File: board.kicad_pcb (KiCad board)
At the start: 2 copper layers, 115.4 x 59.7 mm, 47 parts, among them J1 TEMPS, J2 OLED, J3 HV1, J4 HV2, J5 PWR_IN, J6 PROG, K1 RELAY1, K3 RELAY2, Q3 AO3400A, Q4 AO3400A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

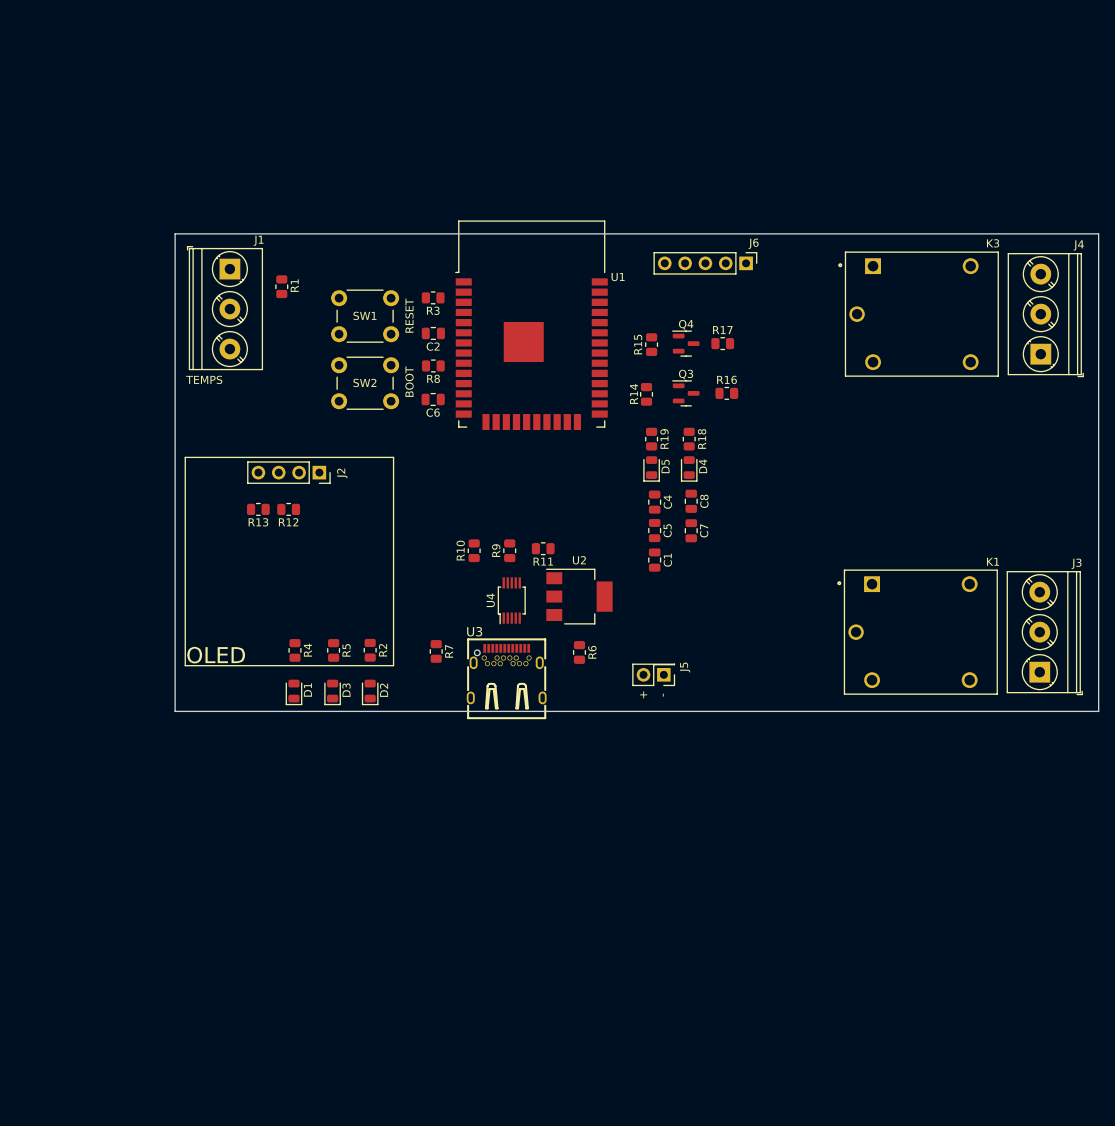
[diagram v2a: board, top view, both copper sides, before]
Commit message: feat: redesigned board for 5x5
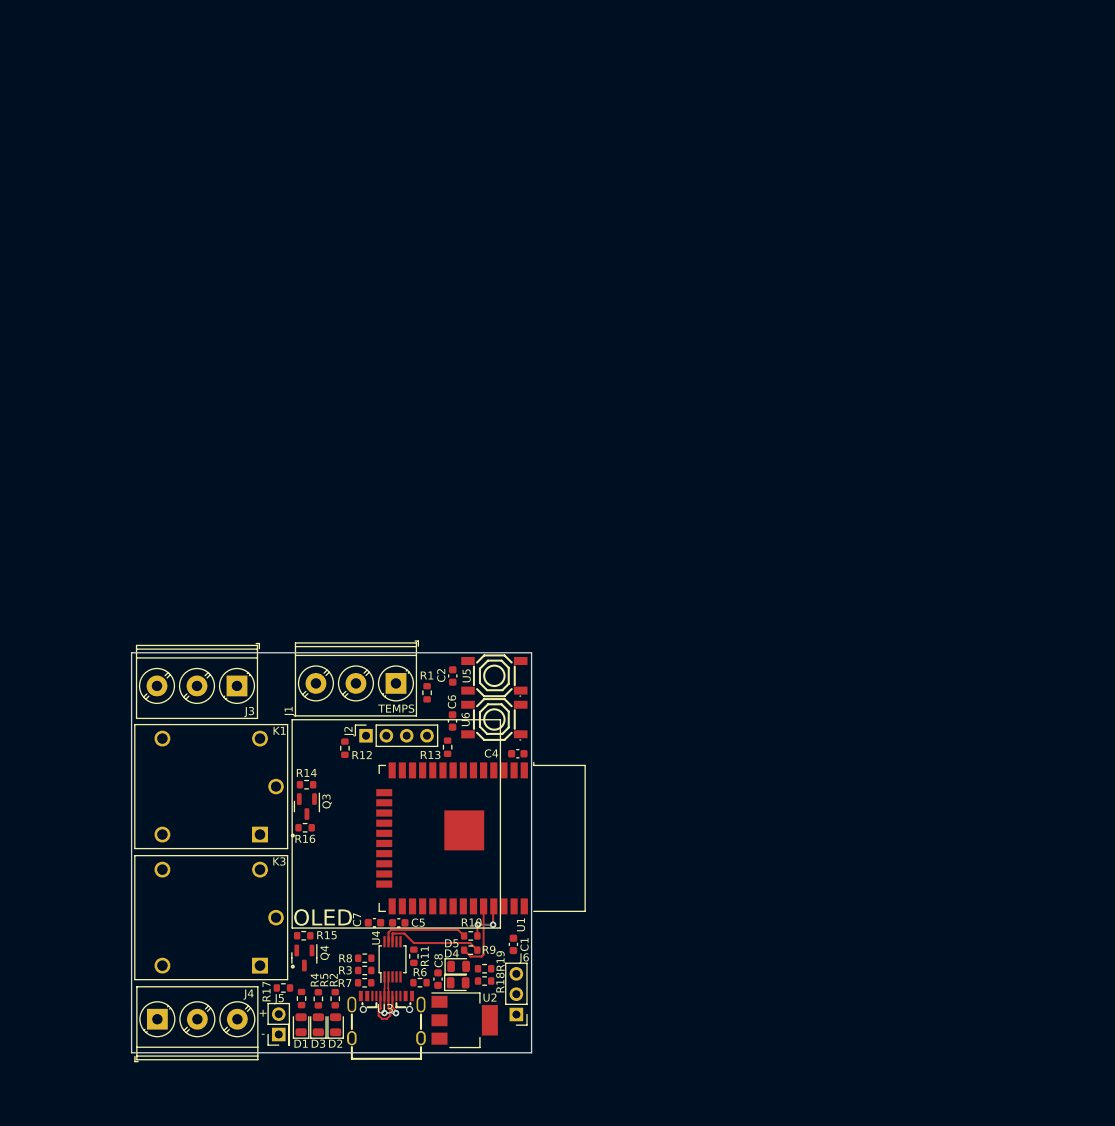
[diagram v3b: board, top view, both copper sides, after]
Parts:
- removed SW1: SW_RST, Button_Switch_THT:SW_PUSH_6mm_H4.3mm
- removed SW2: SW_BOOT, Button_Switch_THT:SW_PUSH_6mm_H4.3mm
- added U5: SW_RST, board:SW-SMD_4P-L5.1-W5.1-P3.70-LS6.5-TL-2, F.Cu at (99.8, 106.2)
- added U6: SW_BOOT, board:SW-SMD_4P-L5.1-W5.1-P3.70-LS6.5-TL-2, F.Cu at (99.8, 111.6)
- C1, C2, C4, C5, C6, C7, C8: footprint Capacitor_SMD:C_0805_2012Metric -> Capacitor_SMD:C_0603_1608Metric
- J6: footprint Connector_PinHeader_2.54mm:PinHeader_1x05_P2.54mm_Vertical -> Connector_PinHeader_2.54mm:PinHeader_1x03_P2.54mm_Vertical
- K1, K3: footprint SRD-05VDC-SL-C:RELAY_SRD-05VDC-SL-C -> board:RELAY_SRD-05VDC-SL-C
- R1, R10, R11, R12, R13, R14, R15, R16, R17, R18, R19, R2, R3, R4, R5, R6, R7, R8, R9: footprint Resistor_SMD:R_0805_2012Metric -> Resistor_SMD:R_0603_1608Metric
- U2: value AMS1117-3.3 -> AMS1117
- U3: value USB-306C -> USB3_1C16PFSMT; footprint board:USB-TYPE-C-TH_USB-306C -> board:USB-C-SMD_TYPE-C-USB-17
- moved J4 138.2 mm to (57.7, 149.1), turned to 0 degrees
- moved K3 116.5 mm to (64.5, 136.4), turned to 180 degrees
- moved J3 100.4 mm to (67.7, 107.4), turned to 180 degrees
- moved J6 98.2 mm to (102.6, 148.5), turned to 180 degrees
- moved R17 97.5 mm to (73.5, 145.2), turned to 180 degrees
- moved K1 90.8 mm to (64.5, 120.0), turned to 180 degrees
- moved Q4 90.4 mm to (76.1, 141.4), turned to -90 degrees
- moved R15 85.7 mm to (76.0, 138.7), turned to 0 degrees
- moved R3 84.5 mm to (83.7, 143.0), turned to 0 degrees
- moved R16 75.7 mm to (76.2, 125.2), turned to 180 degrees
- moved R8 74.5 mm to (83.7, 141.5), turned to 0 degrees
- moved R18 72.4 mm to (98.6, 144.3), turned to 180 degrees
- moved D4 70.6 mm to (95.3, 144.5), turned to 0 degrees
- moved Q3 70.1 mm to (76.4, 122.5), turned to -90 degrees
- moved R19 69.4 mm to (98.6, 142.8), turned to 180 degrees
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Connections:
- net /NCTS renamed NCTS
- net Net-(D4-Pad2) renamed /RXLED_V
- net Net-(D5-Pad2) renamed /TXLED_V
- net Net-(K1-PadA1) renamed /RELAY1_G1
- net Net-(K3-PadA1) renamed /RELAY2_G1
- net Net-(Q3-Pad3) renamed /RELAY1_G2
- net Net-(Q4-Pad3) renamed /RELAY2_G2
- J6 pad 1: +3V3 -> TX_ESP
- J6 pad 3: TX_ESP -> +3V3
- U3 pad A5: CC2 -> CC1
- U3 pad B5: CC1 -> CC2
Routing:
- net TX_CH: track 0.00 -> 12.5 mm
- net RX_CH: track 0.00 -> 11.1 mm
- net RX_ESP: track 0.00 -> 8.89 mm
- net D-: track 0.00 -> 8.53 mm
- net D+: track 0.00 -> 7.60 mm, vias 0 -> 2
- net TX_ESP: track 0.00 -> 5.66 mm, vias 0 -> 2
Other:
- board size 115.4 x 59.7 mm -> 50 x 50 mm
- copper layers 2 -> 4

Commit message: feat: initial routing
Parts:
- J3: value HV1 -> HV2
- J4: value HV2 -> HV1
- K1: value RELAY1 -> RELAY2
- K3: value RELAY2 -> RELAY1
- U2: value AMS1117 -> AMS1117-3.3
- U5, U6: footprint board:SW-SMD_4P-L5.1-W5.1-P3.70-LS6.5-TL-2 -> board:SW-SMD_L6.0-W3.5-LS8.0
- moved J5 12.3 mm to (78.8, 140.2), turned to 180 degrees
- moved R17 11.6 mm to (76.3, 133.9)
- moved Q4 10.2 mm to (76.5, 131.2)
- moved R15 10.2 mm to (76.5, 128.4)
- moved C6 5.53 mm to (93.6, 106.4), turned to 0 degrees
- moved U6 5.25 mm to (99.7, 106.4), turned to 0 degrees
- moved C2 4.16 mm to (93.6, 110.2), turned to 0 degrees
- moved U5 4.05 mm to (99.7, 110.2), turned to 0 degrees
- moved R8 2.46 mm to (82.8, 139.2)
- moved R3 2.45 mm to (82.8, 140.7)
- moved C8 2.15 mm to (92.8, 141.9)
- moved R1 1.85 mm to (91.3, 110.1)
- moved R12 1.24 mm to (81.0, 114.0)
- moved R13 1.12 mm to (93.8, 114.0)
- moved J2 0.64 mm to (83.6, 114.3)
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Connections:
- Q3 pad 1: CH1 -> CH2
- Q4 pad 1: CH2 -> CH1
- R14 pad 2: CH1 -> CH2
- R15 pad 2: CH2 -> CH1
- U5 pad 2: EN_ESP -> GND
- U6 pad 2: GPIO0 -> GND
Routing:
- net Net-(J3-Pad2): track 0.00 -> 103.2 mm
- net Net-(J4-Pad2): track 0.00 -> 100.9 mm
- net VBUS: track 0.00 -> 87.0 mm, vias 0 -> 1
- net Net-(J4-Pad1): track 0.00 -> 80.4 mm
- net Net-(J3-Pad3): track 0.00 -> 80.3 mm
- net GPIO0: track 0.00 -> 60.6 mm, vias 0 -> 2
- net EN_ESP: track 0.00 -> 51.3 mm, vias 0 -> 2
- net Net-(J4-Pad3): track 0.00 -> 48.1 mm
- net Net-(J3-Pad1): track 0.00 -> 48.0 mm
- net SCL: track 0.00 -> 43.0 mm, vias 0 -> 2
- net SLED2: track 0.00 -> 36.3 mm
- net SLED1: track 0.00 -> 34.7 mm
- net SDA: track 0.00 -> 30.5 mm, vias 0 -> 2
- net CH2: track 0.00 -> 29.6 mm, vias 0 -> 2
- net GPIO14: track 0.00 -> 27.0 mm
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
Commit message: feat: routed with planes and no warnings or errors
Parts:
- C1, C2, C4, C5, C6, C7, C8: footprint Capacitor_SMD:C_0603_1608Metric -> Capacitor_SMD:C_0402_1005Metric
- D1, D2, D3, D4, D5: footprint LED_SMD:LED_0805_2012Metric -> LED_SMD:LED_0603_1608Metric
- R1, R10, R11, R12, R13, R14, R15, R16, R17, R18, R19, R2, R3, R4, R5, R6, R7, R8, R9: footprint Resistor_SMD:R_0603_1608Metric -> Resistor_SMD:R_0402_1005Metric
- U3: value USB3_1C16PFSMT -> USBC
- moved J3 100.1 mm to (167.7, 107.1)
- moved K1 98.5 mm to (163.0, 120.2), turned to 0 degrees
- moved Q3 91.3 mm to (166.9, 134.9), turned to 90 degrees
- moved J1 90.8 mm to (167.5, 150.2), turned to 90 degrees
- moved R16 88.9 mm to (164.6, 133.9), turned to -90 degrees
- moved J4 88.2 mm to (135.2, 107.1), turned to 180 degrees
- moved R4 84.9 mm to (159.6, 133.1), turned to 180 degrees
- moved R1 81.8 mm to (162.4, 150.6)
- moved D1 79.6 mm to (153.1, 131.1), turned to 0 degrees
- moved R5 79.5 mm to (156.1, 133.1), turned to 180 degrees
- moved D3 77.2 mm to (153.1, 132.8), turned to 0 degrees
- moved R12 68.1 mm to (148.0, 125.7), turned to 0 degrees
- moved K3 68.0 mm to (130.4, 120.2), turned to 0 degrees
- moved J2 67.0 mm to (139.6, 151.1), turned to 180 degrees
- moved R14 66.5 mm to (139.5, 140.7), turned to -90 degrees
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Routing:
- net Net-(J4-Pad1): track 80.4 -> 34.9 mm
- net Net-(J3-Pad3): track 80.3 -> 34.9 mm
- net +3V3: track 3.37 -> 42.2 mm, vias 0 -> 7
- net EN_ESP: track 51.3 -> 83.7 mm, vias 2 -> 3
- net SLED1: track 34.7 -> 2.86 mm
- net SLED2: track 36.3 -> 7.88 mm
- net GND: track 0.00 -> 19.4 mm, vias 0 -> 11
- net NCTS: track 2.45 -> 20.8 mm, vias 0 -> 2
- net TX_CH: track 19.0 -> 35.1 mm, vias 0 -> 2
- net GPIO0: track 60.6 -> 45.9 mm, vias 2 -> 3
- net TX_ESP: track 18.1 -> 31.7 mm, vias 3 -> 0
- net Net-(J4-Pad3): track 48.1 -> 34.9 mm
- net Net-(J3-Pad2): track 103.2 -> 90.1 mm
- net Net-(J3-Pad1): track 48.0 -> 34.9 mm
- net Net-(J4-Pad2): track 100.9 -> 90.1 mm
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- added copper zone on In2.Cu, net +3V3
- added copper zone on B.Cu, net GND
- added copper zone on F.Cu, net GND
- added copper zone on In1.Cu, net GND
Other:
- board text added: "@wolffshots"

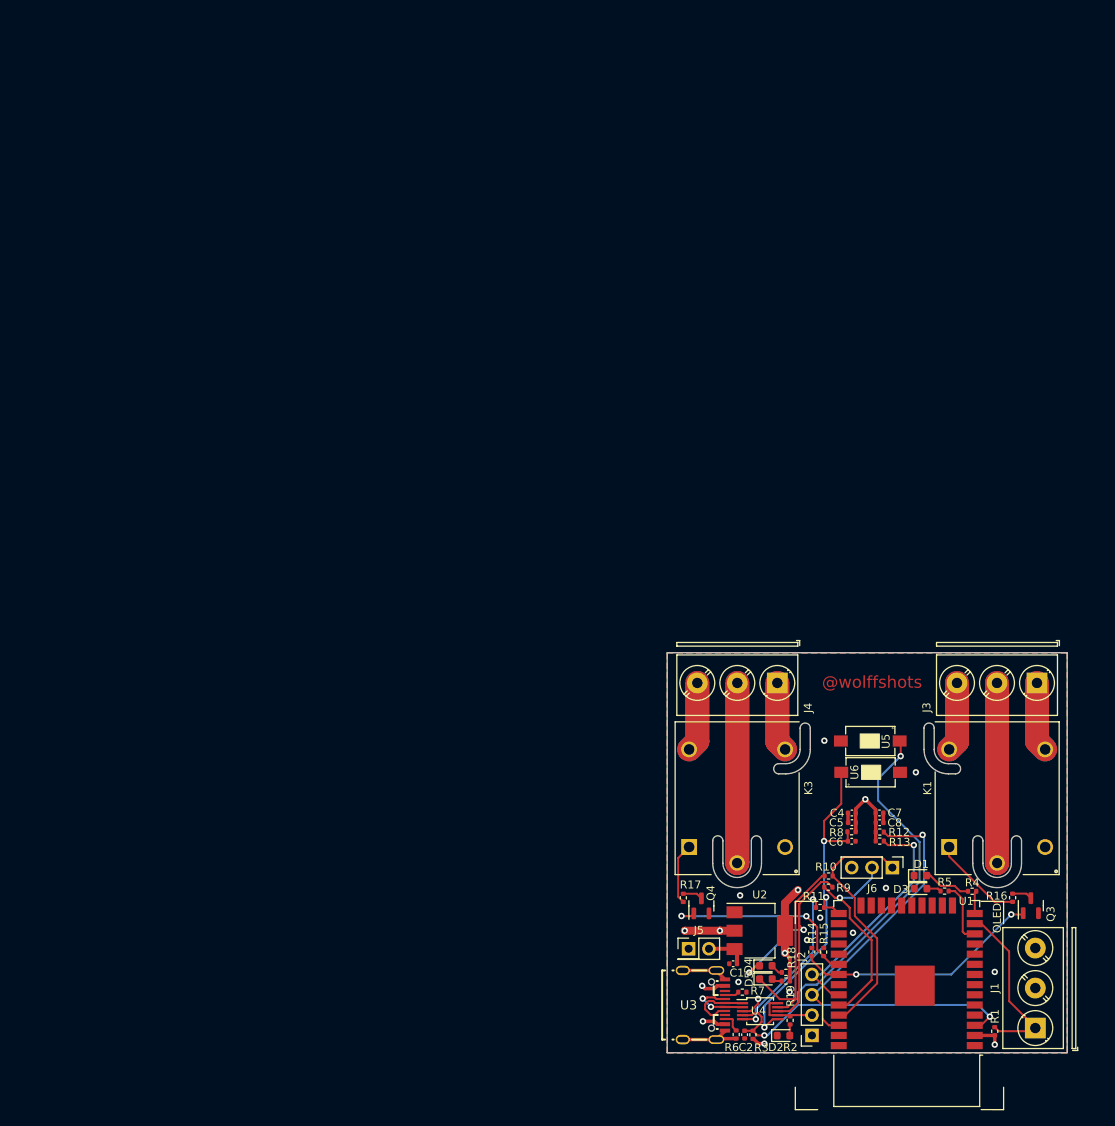
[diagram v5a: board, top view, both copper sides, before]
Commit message: chore: reorganised to respect keepout and corners
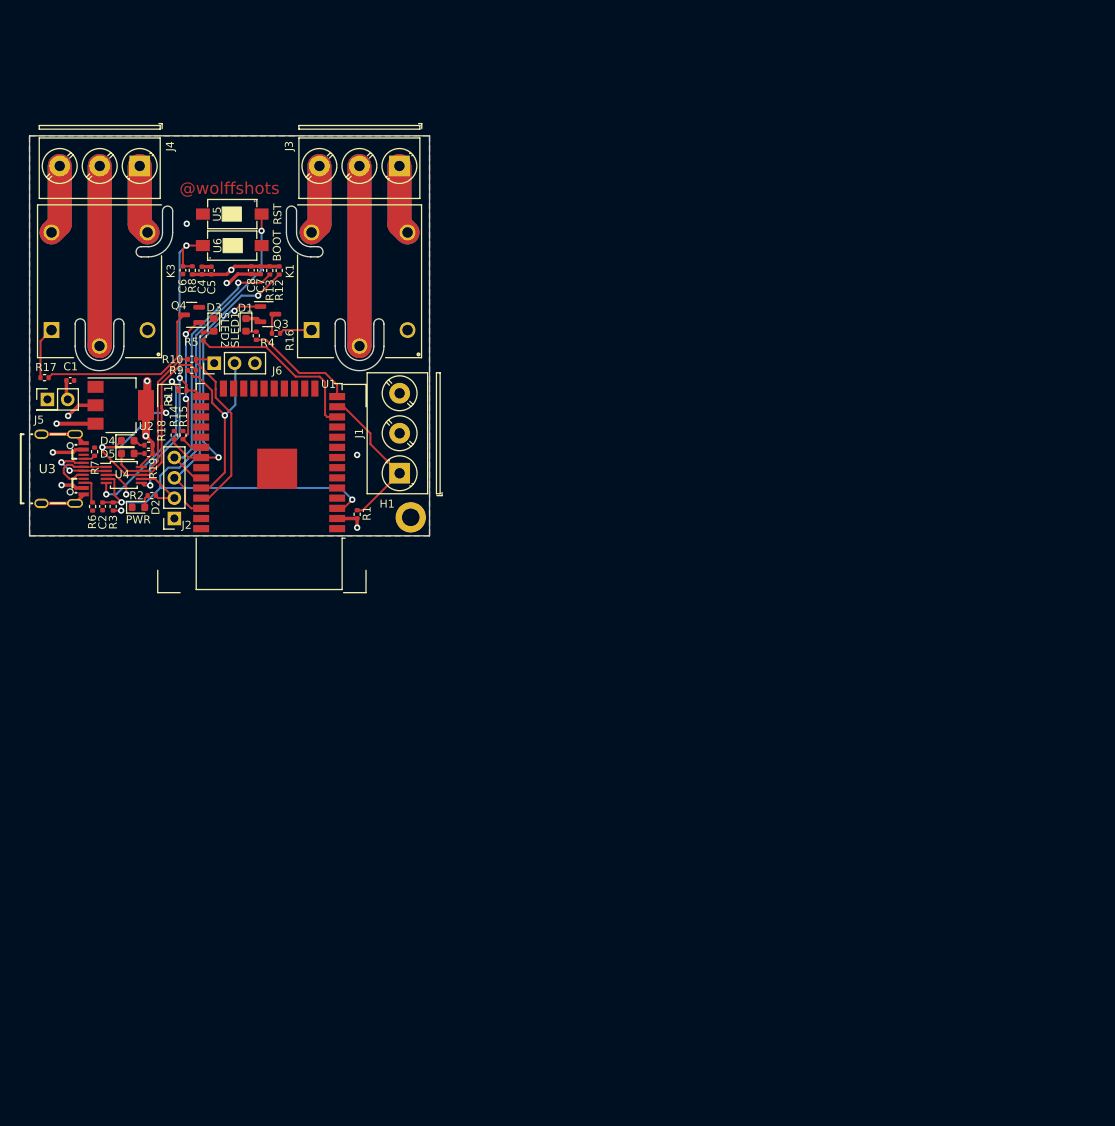
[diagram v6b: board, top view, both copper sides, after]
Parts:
- added H1: MountingHole_Pad, MountingHole:MountingHole_2.2mm_M2_DIN965_Pad, F.Cu at (89.4, 86.4)
- U3: value USBC -> USB3_1C16PFSMT
- moved Q3 120.7 mm to (71.5, 61.0), turned to 0 degrees
- moved R16 116.0 mm to (72.6, 63.4), turned to 0 degrees
- moved R5 115.7 mm to (63.5, 63.8), turned to 90 degrees
- moved R4 113.3 mm to (70.1, 63.7), turned to 90 degrees
- moved D3 113.0 mm to (64.8, 62.3), turned to -90 degrees
- moved C1 110.4 mm to (46.8, 69.2), turned to 180 degrees
- moved C6 109.9 mm to (60.9, 55.5), turned to 90 degrees
- moved D1 108.8 mm to (68.8, 62.3), turned to -90 degrees
- moved R8 108.2 mm to (62.1, 55.5), turned to 90 degrees
- moved C4 105.8 mm to (63.3, 55.5), turned to -90 degrees
- moved C5 105.7 mm to (64.5, 55.5), turned to -90 degrees
- moved J6 105.6 mm to (64.8, 67.1), turned to 90 degrees
- moved J5 105.5 mm to (44.0, 71.6)
- moved J1 105.5 mm to (88.0, 80.8)
- moved R7 105.5 mm to (49.9, 78.2), turned to 90 degrees
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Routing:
- net /RELAY2_G2: track 2.50 -> 22.8 mm
- net SLED2: track 7.88 -> 23.1 mm
- net SLED1: track 2.86 -> 13.9 mm
- net TX_ESP: track 31.7 -> 23.8 mm
- net /RELAY1_G1: track 11.5 -> 4.10 mm
- net CH1: track 24.6 -> 18.5 mm
- net VBUS: track 87.8 -> 82.3 mm, vias 2 -> 3
- net /SLED_V1: track 5.97 -> 1.32 mm
- net EN_ESP: track 83.7 -> 79.5 mm
- net GND: track 19.4 -> 23.7 mm, vias 11 -> 5
- net SDA: track 30.4 -> 34.6 mm
- net TX_CH: track 35.1 -> 38.7 mm
- net RX_CH: track 25.2 -> 21.6 mm
- net +3V3: track 42.2 -> 39.3 mm, vias 7 -> 6
- net GPIO14: track 22.1 -> 19.3 mm
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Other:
- board text removed: "OLED"

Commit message: chore: switched esp footprint
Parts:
- U1: value ESP32-WROOM-32 -> ESP32-WROOM-32D
